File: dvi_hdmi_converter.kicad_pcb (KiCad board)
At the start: 4 copper layers, 3 parts, among them J0 HDMI_A, J1 HDMI_A, J2 DVI-DP-29-C-G-HN-4

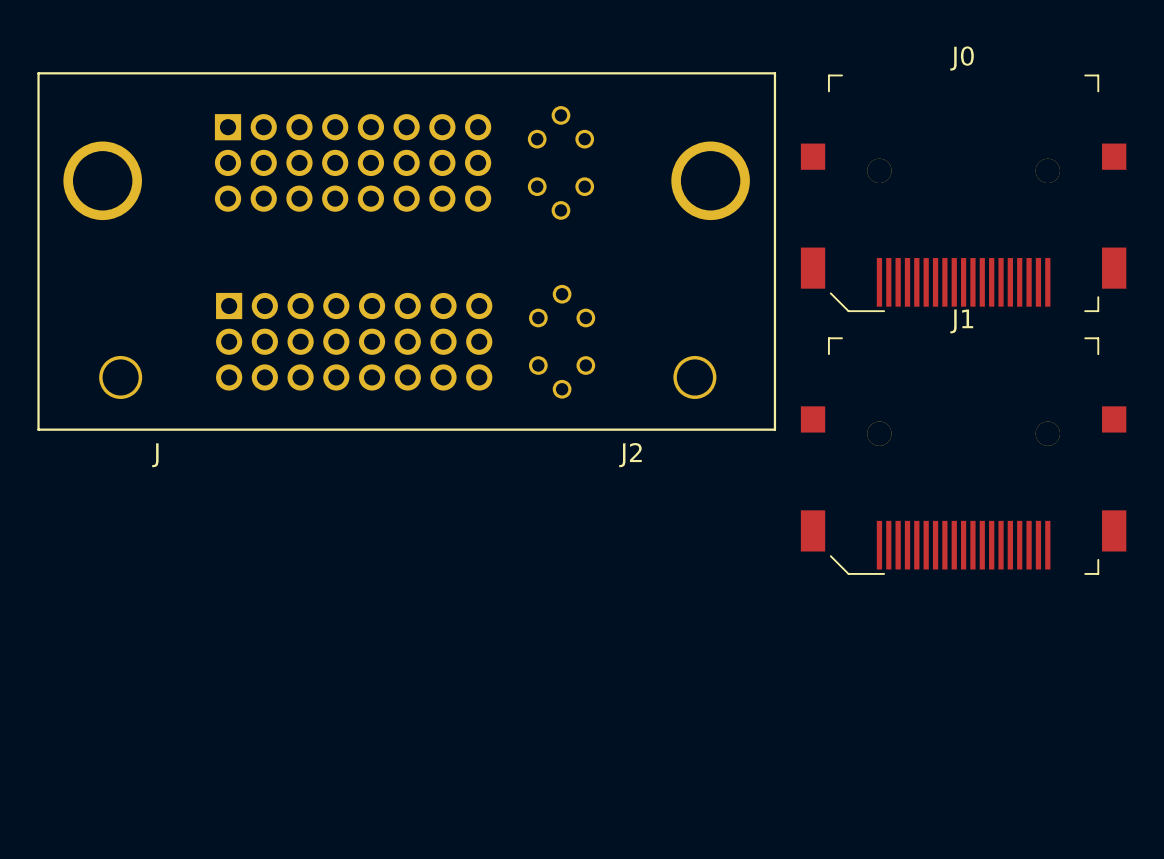
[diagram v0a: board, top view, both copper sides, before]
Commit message: traced out first hdmi port
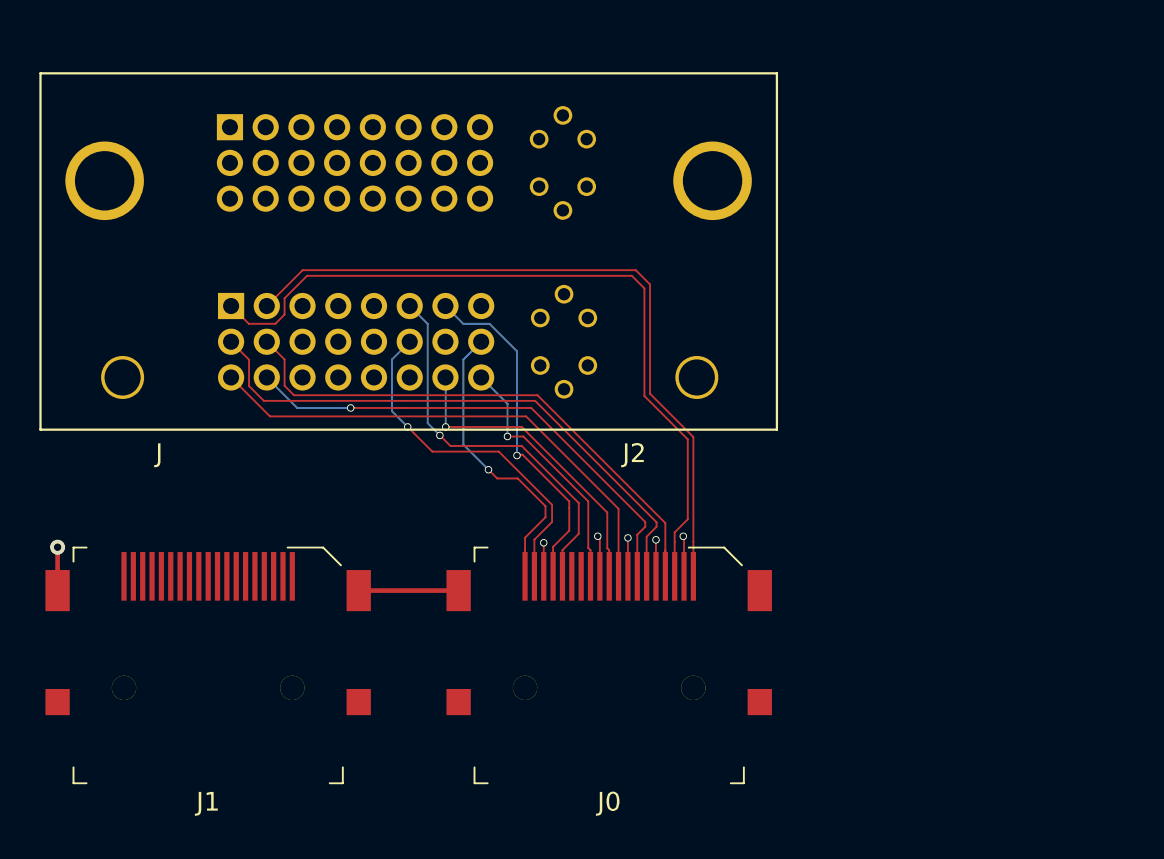
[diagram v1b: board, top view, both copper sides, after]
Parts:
- moved J1 41.8 mm to (114.3, 66.3), turned to 180 degrees
- moved J0 31.1 mm to (135.7, 66.3), turned to 180 degrees
- moved J2 0.10 mm to (126.9, 59.1)
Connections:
- J0 pad SH: /HDMI1SH -> /SH
- J1 pad SH: /HDMI2SH -> /SH
- J2 pad SH1: /HDMI1SH -> /SH
- J2 pad SH2: /HDMI2SH -> /SH
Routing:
- net /HDMI1D2-: track 0.00 -> 41.0 mm
- net /HDMI1D1S: track 0.00 -> 38.3 mm, vias 0 -> 1
- net /HDMI1D2+: track 0.00 -> 38.2 mm
- net /HDMI1D2S: track 0.00 -> 36.3 mm, vias 0 -> 1
- net /HDMI1D0S: track 0.00 -> 36.1 mm, vias 0 -> 1
- net /HDMI1D1-: track 0.00 -> 30.7 mm
- net /HDMI1D1+: track 0.00 -> 30.4 mm
- net /SH: track 0.00 -> 28.3 mm, vias 0 -> 1
- net /HDMI1D0-: track 0.00 -> 27.2 mm
- net /HDMI1D0+: track 0.00 -> 26.5 mm, vias 0 -> 1
- net /HDMI1SCL: track 0.00 -> 20.8 mm, vias 0 -> 1
- net /HDMI1GND: track 0.00 -> 20.7 mm, vias 0 -> 1
- net /HDMI15V: track 0.00 -> 19.0 mm, vias 0 -> 1
- net /HDMI1SDA: track 0.00 -> 18.6 mm, vias 0 -> 1
- net /HDMI1HPD: track 0.00 -> 17.3 mm, vias 0 -> 1
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
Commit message: created first version of the layout
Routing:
- net /HDMI2D0-: track 0.00 -> 54.5 mm
- net /HDMI2CK-: track 0.00 -> 51.1 mm
- net /HDMI2GND: track 0.00 -> 50.8 mm, vias 0 -> 1
- net /HDMI2CK+: track 0.00 -> 48.3 mm
- net /HDMI2D0+: track 0.00 -> 46.6 mm
- net /HDMI2CKS: track 0.00 -> 45.8 mm, vias 0 -> 1
- net /HDMI2SDA: track 0.00 -> 42.0 mm, vias 0 -> 1
- net /HDMI2SCL: track 0.00 -> 39.7 mm, vias 0 -> 1
- net /HDMI2HPD: track 0.00 -> 37.4 mm, vias 0 -> 1
- net /HDMI2D1+: track 0.00 -> 35.5 mm
- net /HDMI25V: track 0.00 -> 34.8 mm, vias 0 -> 1
- net /HDMI2D1-: track 0.00 -> 34.6 mm, vias 0 -> 1
- net /HDMI2D2S: track 0.00 -> 33.9 mm, vias 0 -> 1
- net /HDMI2D1S: track 0.00 -> 29.4 mm, vias 0 -> 1
- net /HDMI2D2+: track 0.00 -> 28.3 mm
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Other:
- net class Diff_Traces removed
- net class Standard_Traces removed
- rule trace_min: 0.2 -> 0.01

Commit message: latest update with schematic
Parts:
- J2: footprint footprints:DVI-DP-29-C-G-HN-4 -> footprints:DVI-DP-29-C-G-HN-4-no-analog
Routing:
- net /HDMI2D0-: track 54.5 -> 0.00 mm
- net /HDMI2CK-: track 51.1 -> 0.00 mm
- net /HDMI2GND: track 50.8 -> 0.00 mm, vias 1 -> 0
- net /HDMI2CK+: track 48.3 -> 0.00 mm
- net /HDMI2D0+: track 46.6 -> 0.00 mm
- net /HDMI2CKS: track 45.8 -> 0.00 mm, vias 1 -> 0
- net /HDMI2SDA: track 42.0 -> 0.00 mm, vias 1 -> 0
- net /HDMI1D2-: track 41.0 -> 0.00 mm
- net /HDMI2SCL: track 39.7 -> 0.00 mm, vias 1 -> 0
- net /HDMI1D1S: track 38.3 -> 0.00 mm, vias 1 -> 0
- net /HDMI1D2+: track 38.2 -> 0.00 mm
- net /HDMI2HPD: track 37.4 -> 0.00 mm, vias 1 -> 0
- net /HDMI1D2S: track 36.3 -> 0.00 mm, vias 1 -> 0
- net /HDMI1D0S: track 36.1 -> 0.00 mm, vias 1 -> 0
- net /HDMI2D1+: track 35.5 -> 0.00 mm
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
